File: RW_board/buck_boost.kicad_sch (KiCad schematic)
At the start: 0 parts

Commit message: Implemented Initial Schematic of Boost Converter
Some part values not fully defined but expected footprint added
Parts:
- added C10, C15, C19: 100n, Capacitor_SMD:C_0402_1005Metric_Pad0.74x0.62mm_HandSolder, symbol Device:C
- added C11, C16, C17, C20, C8: 10u, Capacitor_SMD:C_0603_1608Metric_Pad1.08x0.95mm_HandSolder, symbol Device:C
- added C12: 10n, Capacitor_SMD:C_0402_1005Metric_Pad0.74x0.62mm_HandSolder, symbol Device:C
- added C13, C18, C9: 1u, Capacitor_SMD:C_0402_1005Metric_Pad0.74x0.62mm_HandSolder, symbol Device:C
- added C14: 10p, Capacitor_SMD:C_0402_1005Metric_Pad0.74x0.62mm_HandSolder, symbol Device:C
- added C6: 1n, Capacitor_SMD:C_0402_1005Metric_Pad0.74x0.62mm_HandSolder, symbol Device:C
- added D1: SDM2U30CSP-7, X3-WLB1608-2, symbol Senior Design:SDM2U30CSP-7
- added L1: XGL4040-223MEC, XGL4040-223MEC:IND_XGL4040-223MEC, symbol XGLInductor:XGL4040-223MEC
- added Q1: BSZ300N15NS5ATMA1, BSZ300N15NS5ATMA1, symbol Senior Design:BSZ300N15NS5ATMA1
- added R10: 390m, Resistor_SMD:R_0805_2012Metric_Pad1.20x1.40mm_HandSolder, symbol Device:R
- added R11: 10k, Resistor_SMD:R_0402_1005Metric, symbol Device:R
- added R12: 3.01k, Resistor_SMD:R_0402_1005Metric, symbol Device:R
- added R13: 24k, Resistor_SMD:R_0402_1005Metric, symbol Device:R
- added R14: 1.33k, Resistor_SMD:R_0402_1005Metric, symbol Device:R
- added R15: 1.1k, Resistor_SMD:R_0402_1005Metric, symbol Device:R
- added R7: 16k, Resistor_SMD:R_0402_1005Metric, symbol Device:R
- added R8: 6.9k, Resistor_SMD:R_0402_1005Metric, symbol Device:R
- added R9: 100, Resistor_SMD:R_0402_1005Metric, symbol Device:R
- added U1: LM5022MM, Package_SO:MSOP-10_3x3mm_P0.5mm, symbol Regulator_Switching:LM5022MM
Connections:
- new net: C14.1, C15.1, R13.1, R14.2, U1.2 (FB)
- new net: C15.2, R15.1
- new net: C6.1, R8.2, R9.1
- new net: C14.2, R15.2, U1.3 (COMP)
- new net: R11.2, R12.1, U1.7 (UVLO)
- new net: C13.1, U1.4 (VCC)
- new net: L1.2, Q1.4 (GATE), U1.5 (OUT)
- new net: C12.1, U1.10 (SS)
- new net: R8.1, U1.8 (CS)
- new net: R7.1, U1.9 (RT)
- new net 24V: C16.1, C17.1, C18.1, C19.1, C20.1, D1.1 (K), R13.2
- new net BattIn: C10.1, C11.1, C8.1, C9.1, L1.1, R11.1, U1.1 (VIN)
- new net Drain: D1.2 (A), Q1.10 (DRAIN_5), Q1.5 (DRAIN_1), Q1.6 (DRAIN_2), Q1.7 (DRAIN_3), Q1.8 (DRAIN_4)
- new net GND: C10.2, C11.2, C12.2, C13.2, C16.2, C17.2, C18.2, C19.2, C20.2, C6.2, C8.2, C9.2, R10.1, R12.2, R14.1, R7.2, U1.6 (GND)
- new net Source: Q1.1 (SOURCE_1), Q1.2 (SOURCE_2), Q1.3 (SOURCE_3), Q1.9 (SOURCE_4), R10.2, R9.2
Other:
- note added: "RL1220S-R39-F"

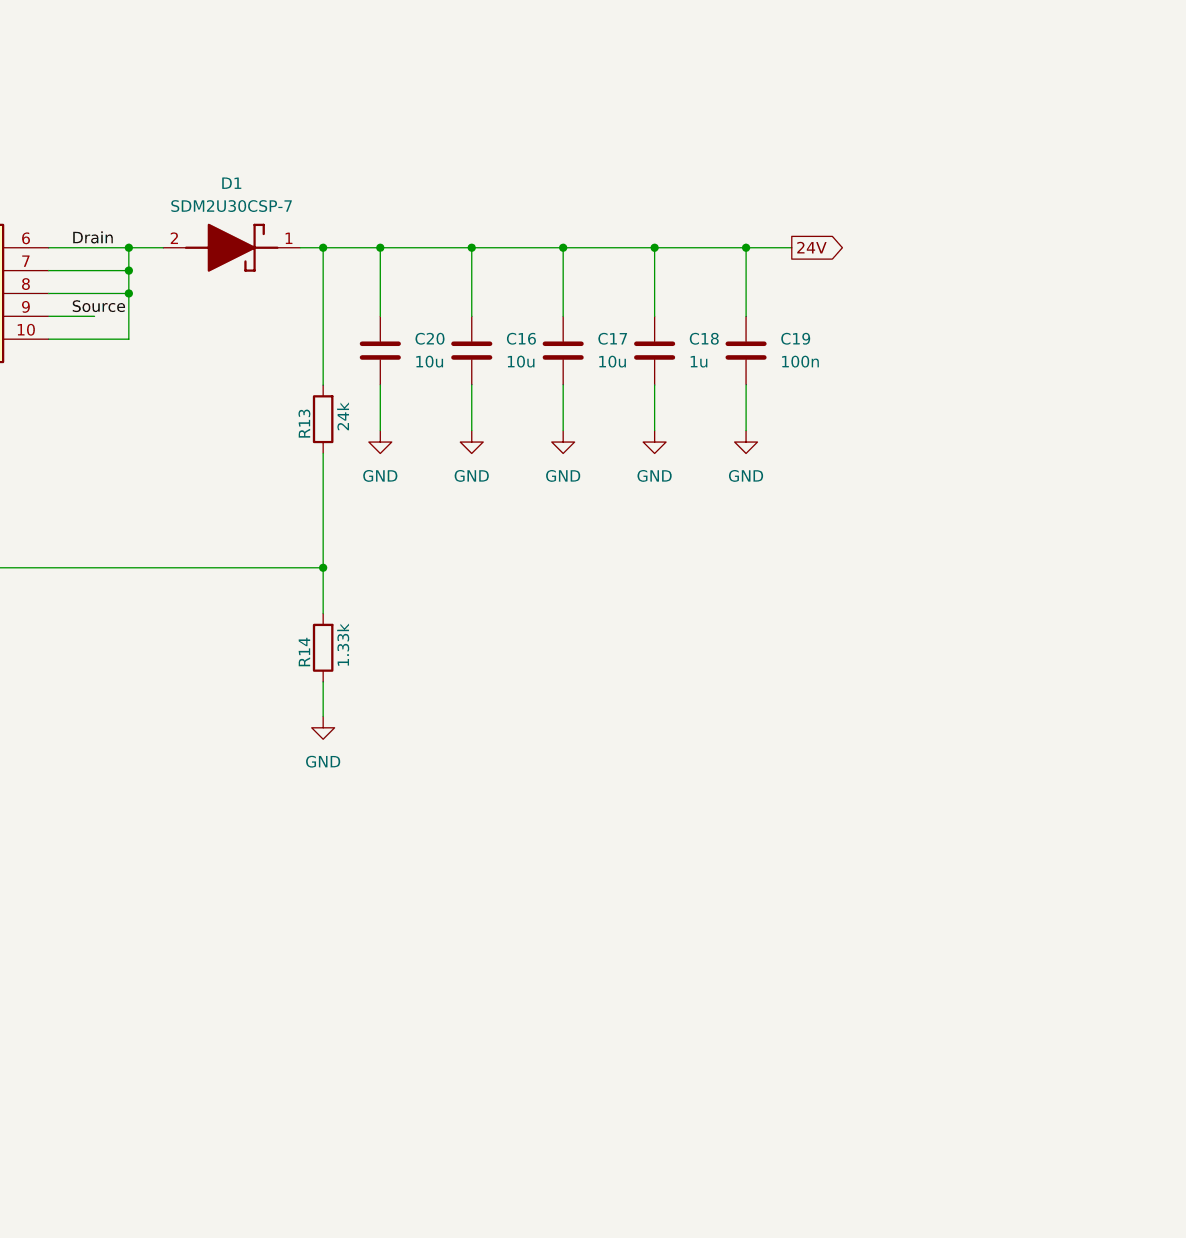
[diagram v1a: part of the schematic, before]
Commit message: Boost Converter Update: V & C Sense
Added voltage and current sensing
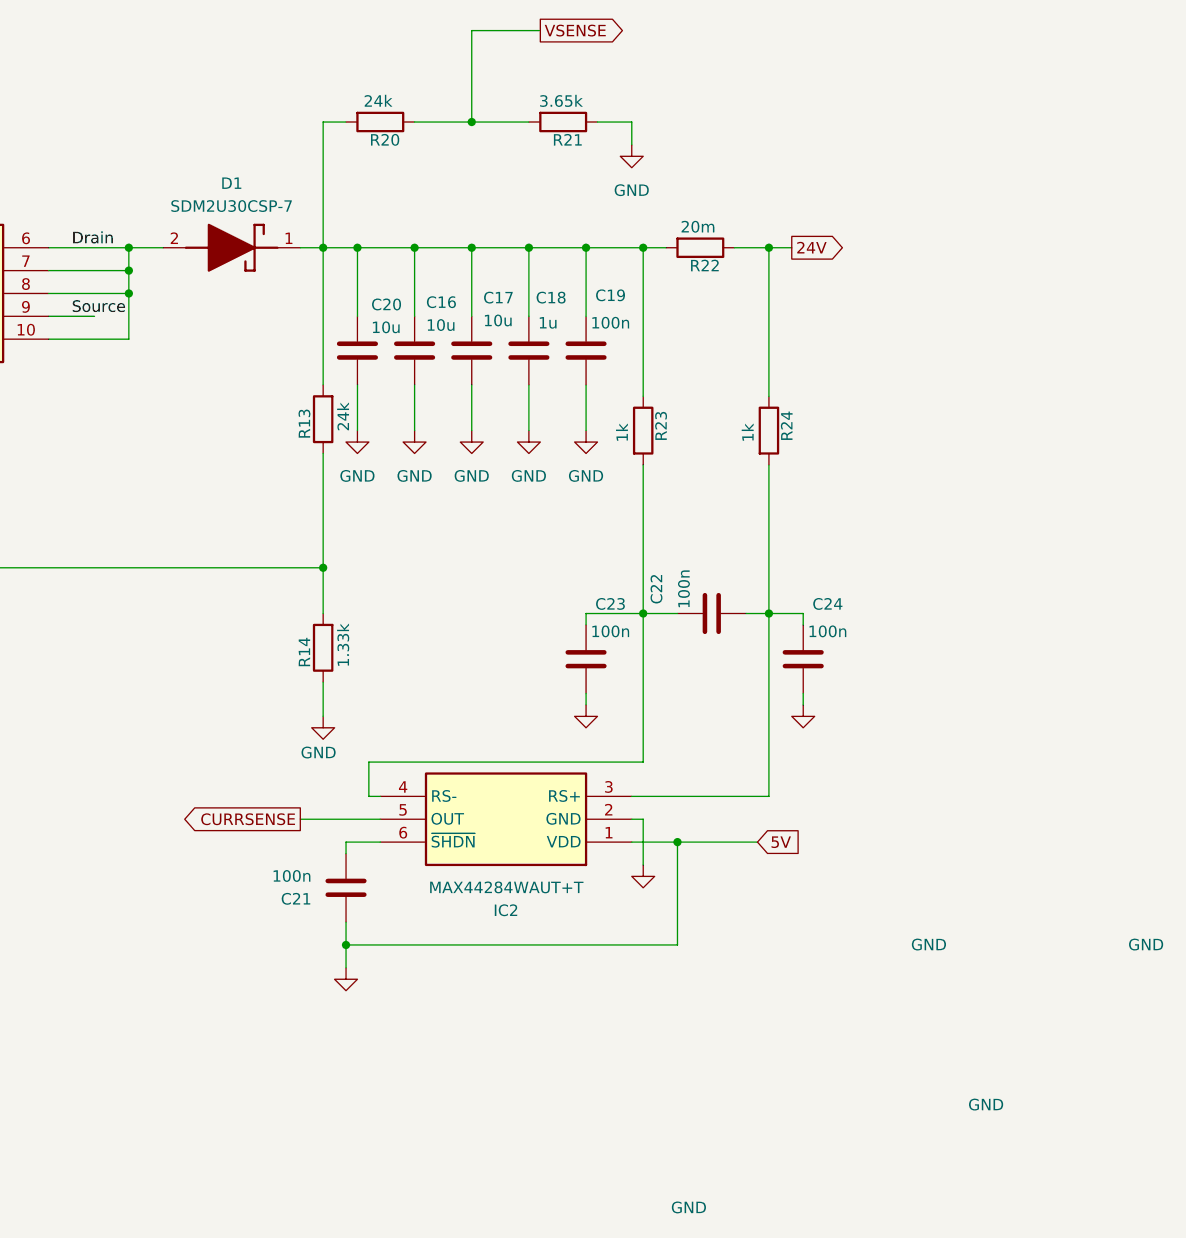
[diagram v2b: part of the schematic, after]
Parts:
- added C21, C22, C23, C24: 100n, Capacitor_SMD:C_0402_1005Metric_Pad0.74x0.62mm_HandSolder, symbol Device:C
- added IC2: MAX44284WAUT+T, SOT95P280X145-6N, symbol Senior Design:MAX44284WAUT+T
- added R20: 24k, Resistor_SMD:R_0402_1005Metric, symbol Device:R
- added R21: 3.65k, Resistor_SMD:R_0402_1005Metric, symbol Device:R
- added R22: 20m, Capacitor_SMD:C_0201_0603Metric_Pad0.64x0.40mm_HandSolder, symbol Device:R
- added R23, R24: 1k, Resistor_SMD:R_0402_1005Metric, symbol Device:R
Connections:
- net 24V: now also R22.1, R24.1; no longer C16.1, C17.1, C18.1, C19.1, C20.1, D1.1 (K), R13.2
- net GND: now also C21.1, C23.2, C24.2, IC2.1 (VDD), IC2.2 (GND), R21.1
- new net: C22.2, C24.1, IC2.3 (RS+), R24.2
- new net: C16.1, C17.1, C18.1, C19.1, C20.1, D1.1 (K), R13.2, R20.2, R22.2, R23.1
- new net: C22.1, C23.1, IC2.4 (RS-), R23.2
- new net: C21.2, IC2.6 (~{SHDN})
- new net CURRSENSE: IC2.5 (OUT)
- new net VSENSE: R20.1, R21.2
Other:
- moved on the sheet: C16, C17, C18, C19, C20

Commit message: Connected everything, added testpoints
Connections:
- net 24V renamed 24V_OUT
- net CURRSENSE renamed CURRENTSENSE
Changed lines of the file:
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@@
 	(label "Drain"
 		(at 153.67 53.34 0)
-		(fields_autoplaced yes)
 		(effects
 			(font
@@
 	(label "Source"
 		(at 198.12 50.8 0)
-		(fields_autoplaced yes)
 		(effects
 			(font
@@
 	(label "Drain"
 		(at 198.12 43.18 0)
-		(fields_autoplaced yes)
 		(effects
 			(font
@@
 	(label "Source"
 		(at 146.05 43.18 0)
-		(fields_autoplaced yes)
 		(effects
 			(font
@@
 		)
 	)
-	(global_label "BattIn"
+	(hierarchical_label "5V"
 		(shape input)
-		(at 22.86 50.8 180)
-		(fields_autoplaced yes)
+		(at 274.32 109.22 0)
+		(effects
+			(font
+				(size 1.27 1.27)
+			)
+			(justify left)
+		)
+	)
+	(hierarchical_label "VSENSE"
+		(shape output)
+		(at 250.19 19.05 0)
+		(effects
+			(font
+				(size 1.27 1.27)
+			)
+			(justify left)
+		)
+	)
+	(hierarchical_label "CURRENTSENSE"
+		(shape output)
+		(at 223.52 106.68 180)
 		(effects
 			(font
@@
 			(justify right)
 		)
-		(property "Intersheetrefs" "${INTERSHEET_REFS}"
-			(at 14.2506 50.8 0)
-			(effects
-				(font
-					(size 1.27 1.27)
-				)
-				(justify right)
-				(hide yes)
+	)
+	(hierarchical_label "BattIn"
+		(shape input)
+		(at 22.86 50.8 180)
+		(effects
+			(font
+				(size 1.27 1.27)
 			)
+			(justify right)
 		)
 	)
-	(global_label "VSENSE"
+	(hierarchical_label "24V_OUT"
 		(shape output)
-		(at 250.19 19.05 0)
-		(fields_autoplaced yes)
+		(at 278.13 43.18 0)
 		(effects
 			(font
@@
 			(justify left)
 		)
-		(property "Intersheetrefs" "${INTERSHEET_REFS}"
-			(at 260.3113 19.05 0)
-			(effects
-				(font
-					(size 1.27 1.27)
-				)
-				(justify left)
-				(hide yes)
-			)
-		)
 	)
-	(global_label "CURRSENSE"
-		(shape output)
-		(at 223.52 106.68 180)
-		(fields_autoplaced yes)
-		(effects
-			(font
-				(size 1.27 1.27)
-			)
-			(justify right)
-		)
-		(property "Intersheetrefs" "${INTERSHEET_REFS}"
-			(at 209.3468 106.68 0)
-			(effects
-				(font
-					(size 1.27 1.27)
-				)
-				(justify right)
-				(hide yes)
-			)
-		)
-	)
-	(global_label "5V"
-		(shape input)
-		(at 274.32 109.22 0)
-		(fields_autoplaced yes)
-		(effects
-			(font
-				(size 1.27 1.27)
-			)
-			(justify left)
-		)
-		(property "Intersheetrefs" "${INTERSHEET_REFS}"
-			(at 279.6033 109.22 0)
-			(effects
-				(font
-					(size 1.27 1.27)
-				)
-				(justify left)
-				(hide yes)
-			)
-		)
-	)
-	(global_label "24V"
-		(shape output)
-		(at 278.13 43.18 0)
-		(fields_autoplaced yes)
-		(effects
-			(font
-				(size 1.27 1.27)
-			)
-			(justify left)
-		)
-		(property "Intersheetrefs" "${INTERSHEET_REFS}"
-			(at 289.6422 43.18 0)
-			(effects
-				(font
-					(size 1.27 1.27)
-				)
-				(justify left)
-				(hide yes)
-			)
-		)
-	)

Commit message: Initial board layout
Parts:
- removed C21: 100n, Capacitor_SMD:C_0402_1005Metric_Pad0.74x0.62mm_HandSolder, symbol Device:C
- added C210: 100n, Capacitor_SMD:C_0402_1005Metric_Pad0.74x0.62mm_HandSolder, symbol Device:C
- L201: renamed from L1; footprint XGL4040-223MEC:IND_XGL4040-223MEC -> RW_Imports:IND_XGL4040-223MEC
- R213: renamed from R22; footprint Capacitor_SMD:C_0201_0603Metric_Pad0.64x0.40mm_HandSolder -> Capacitor_SMD:C_0603_1608Metric
- renumbered C11 to C201, C8 to C202, C9 to C203, C10 to C204, C12 to C205, C13 to C206, C15 to C207, C6 to C208, C14 to C209, C20 to C211, C16 to C212, C17 to C213, C18 to C214, C19 to C215, C23 to C216, C22 to C217, C24 to C218, D1 to D201, IC2 to IC201, Q1 to Q201, R7 to R201, R11 to R202, R12 to R203, R15 to R204, R8 to R205, R9 to R206, R10 to R207, R13 to R208, R14 to R209, R20 to R210, R21 to R211, R23 to R212, R24 to R214, U1 to U201
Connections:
- net GND: now also IC201.6 (~{SHDN}), C210.1; no longer IC201.1 (VDD)
- new net 5V: C210.2, IC201.1 (VDD)

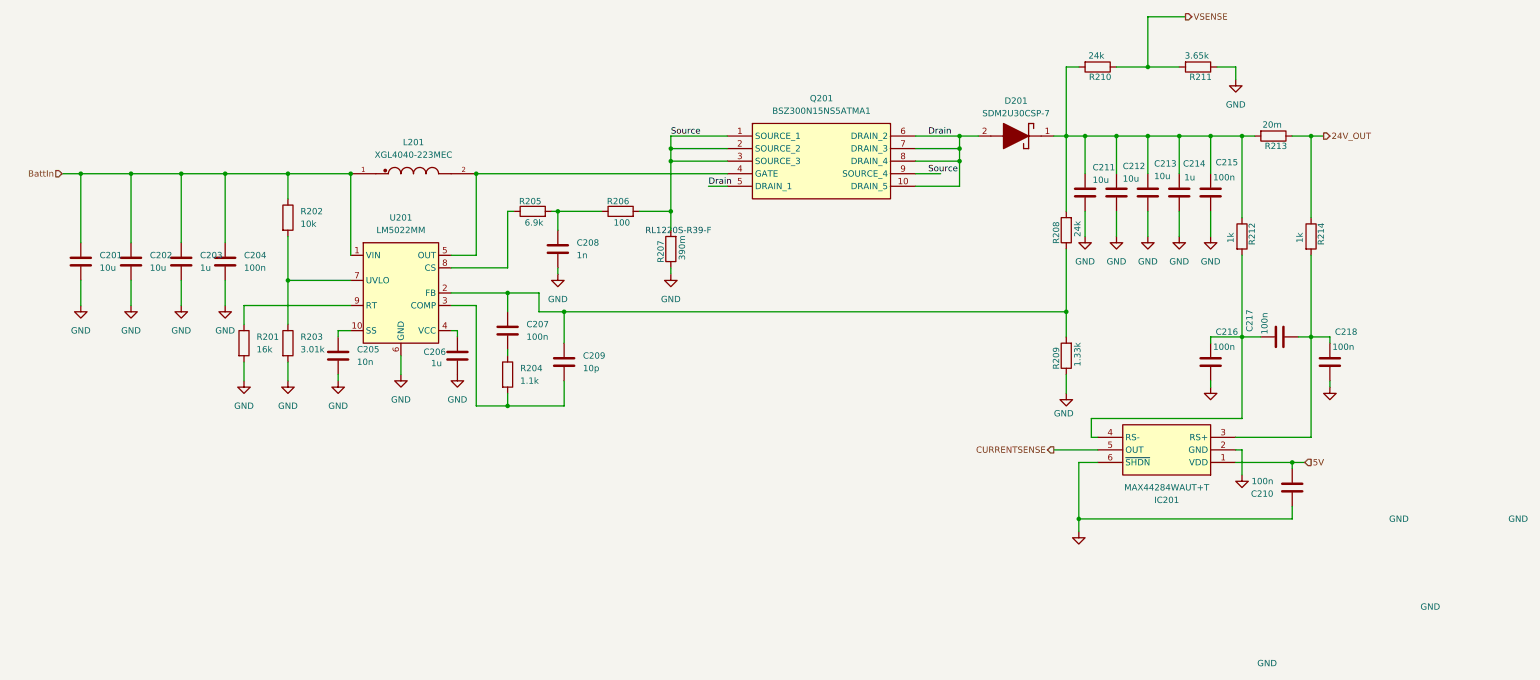
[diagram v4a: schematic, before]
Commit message: Fixed some Boost sillyness
Added Testpoints, another cap for Curr sense IC, and fixed mosfet pinout
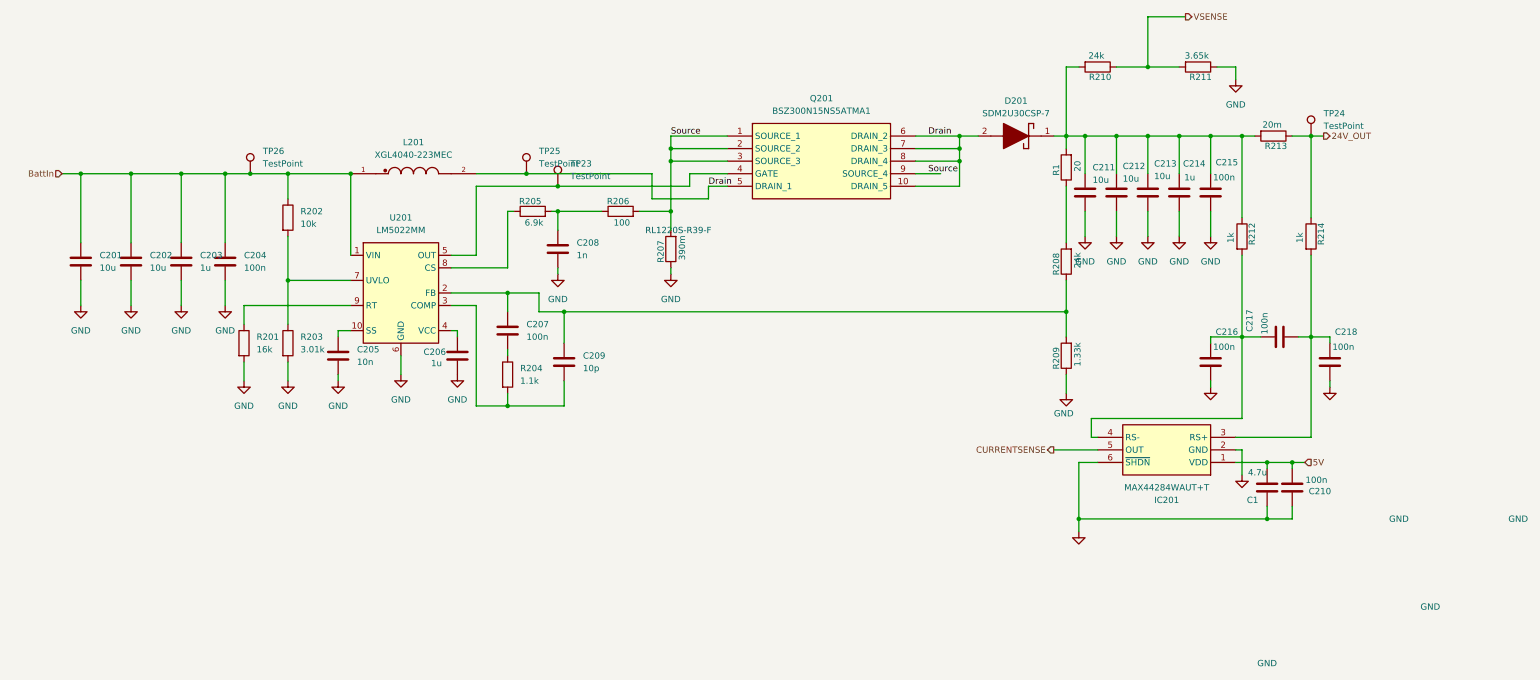
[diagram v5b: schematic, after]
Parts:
- added C1: 4.7u, Capacitor_SMD:C_0402_1005Metric_Pad0.74x0.62mm_HandSolder, symbol Device:C
- added R1: 20, Resistor_SMD:R_0402_1005Metric, symbol Device:R
- added TP23, TP24, TP25, TP26: TestPoint, symbol Connector:TestPoint
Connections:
- net 24V_OUT: now also TP24.1
- net 5V: now also C1.2
- net BattIn: now also TP26.1
- net Drain: now also L201.2, TP25.1
- net GND: now also C1.1
- net at C211.1, C212.1, C213.1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: now also R1.2; no longer R208.2
- net at Q201.4 (GATE), U201.5 (OUT): now also TP23.1; no longer L201.2
- new net: R1.1, R208.2
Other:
- moved on the sheet: R208

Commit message: Some more boost changes
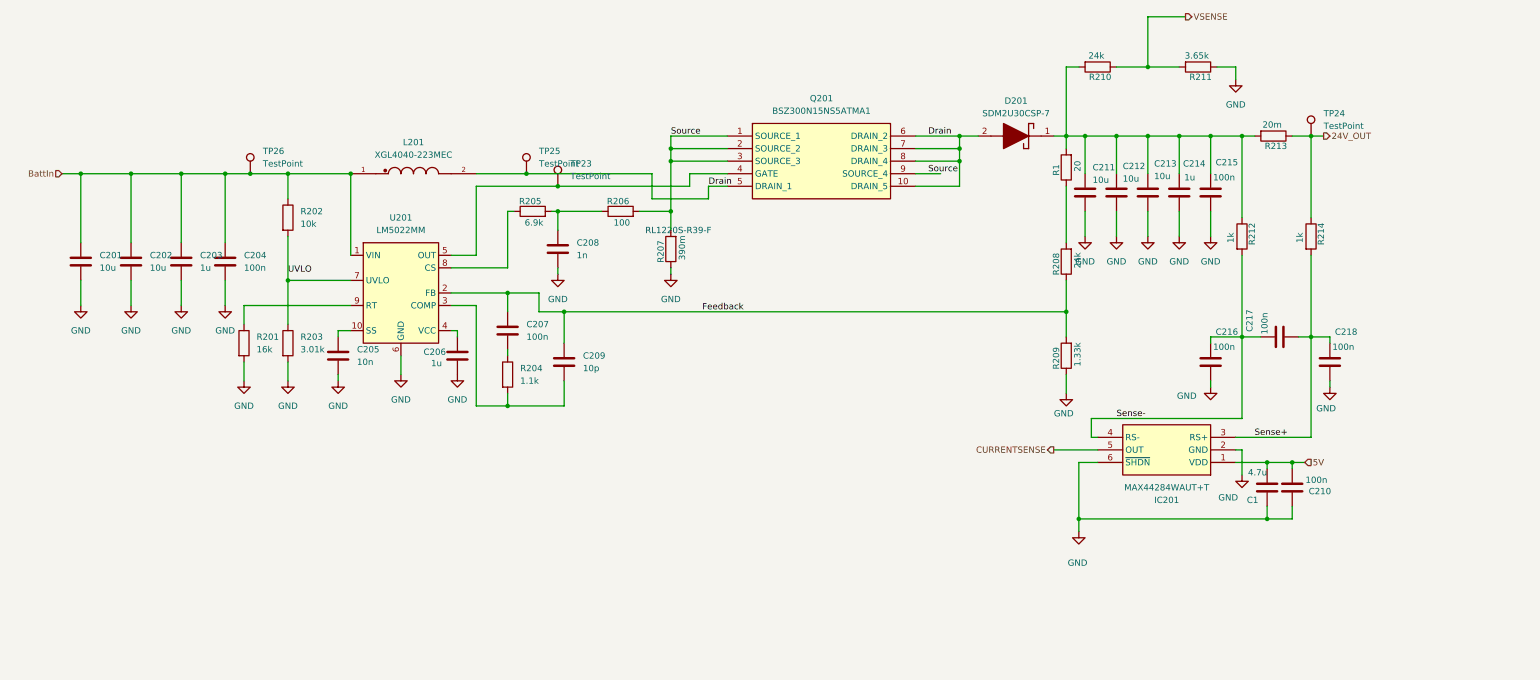
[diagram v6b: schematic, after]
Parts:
- TP23, TP24, TP25, TP26: footprint (none) -> TestPoint:TestPoint_Pad_1.0x1.0mm
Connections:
- net Sense+: now reaches C217.2, C218.1, IC201.3 (RS+), R214.2
- net Feedback: now reaches C207.1, C209.1, R208.1, R209.2, U201.2 (FB)
- net UVLO: now reaches R202.2, R203.1, U201.7 (UVLO)
- net Sense-: now reaches C216.1, C217.1, IC201.4 (RS-), R212.2
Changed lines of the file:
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@@
 		)
 	)
+	(label "UVLO"
+		(at 68.58 71.12 0)
+		(fields_autoplaced yes)
+		(effects
+			(font
+				(size 1.27 1.27)
+			)
+			(justify left bottom)
+		)
+	)
+	(label "Sense-"
+		(at 236.22 100.33 0)
+		(fields_autoplaced yes)
+		(effects
+			(font
+				(size 1.27 1.27)
+			)
+			(justify left bottom)
+		)
+	)
 	(label "Drain"
 		(at 198.12 43.18 0)
@@
 		)
 	)
+	(label "Sense+"
+		(at 264.16 104.14 0)
+		(fields_autoplaced yes)
+		(effects
+			(font
+				(size 1.27 1.27)
+			)
+			(justify left bottom)
+		)
+	)
+	(label "Feedback"
+		(at 152.4 78.74 0)
+		(fields_autoplaced yes)
+		(effects
+			(font
+				(size 1.27 1.27)
+			)
+			(justify left bottom)
+		)
+	)
 	(hierarchical_label "5V"
 		(shape input)
@@
 		)
 		(property "Value" "GND"
-			(at 299.72 138.43 0)
+			(at 258.826 116.332 0)
 			(effects
 				(font
@@
 		)
 		(property "Value" "GND"
-			(at 293.37 120.65 0)
+			(at 250.444 95.758 0)
 			(effects
 				(font
@@
 			)
 		)
-		(property "Footprint" ""
+		(property "Footprint" "TestPoint:TestPoint_Pad_1.0x1.0mm"
 			(at 128.27 53.34 0)
 			(effects
@@
 			)
 		)
-		(property "Footprint" ""
+		(property "Footprint" "TestPoint:TestPoint_Pad_1.0x1.0mm"
 			(at 280.67 43.18 0)
 			(effects
@@
 		)
 		(property "Value" "GND"
-			(at 266.7 149.86 0)
+			(at 228.346 129.54 0)
 			(effects
 				(font
@@
 			)
 		)
-		(property "Footprint" ""
+		(property "Footprint" "TestPoint:TestPoint_Pad_1.0x1.0mm"
 			(at 121.92 50.8 0)
 			(effects
@@
 			)
 		)
-		(property "Footprint" ""
+		(property "Footprint" "TestPoint:TestPoint_Pad_1.0x1.0mm"
 			(at 66.04 50.8 0)
 			(effects
@@
 		)
 		(property "Value" "GND"
-			(at 317.5 120.65 0)
+			(at 278.638 98.298 0)
 			(effects
 				(font
